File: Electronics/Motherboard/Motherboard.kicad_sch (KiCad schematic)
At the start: 55 parts, among them J1 DX07S024JJ3R1300, J2 Conn_02x10_Odd_Even, M1 AO3400A, M2 AO3400A, M3 AO3400A, U1 AMS1117-3.3, U2 TMC2209_SILENTSTEPSTICK, U3 TMC2209_SILENTSTEPSTICK, U4 TMC2209_SILENTSTEPSTICK, U5 TMC2209_SILENTSTEPSTICK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

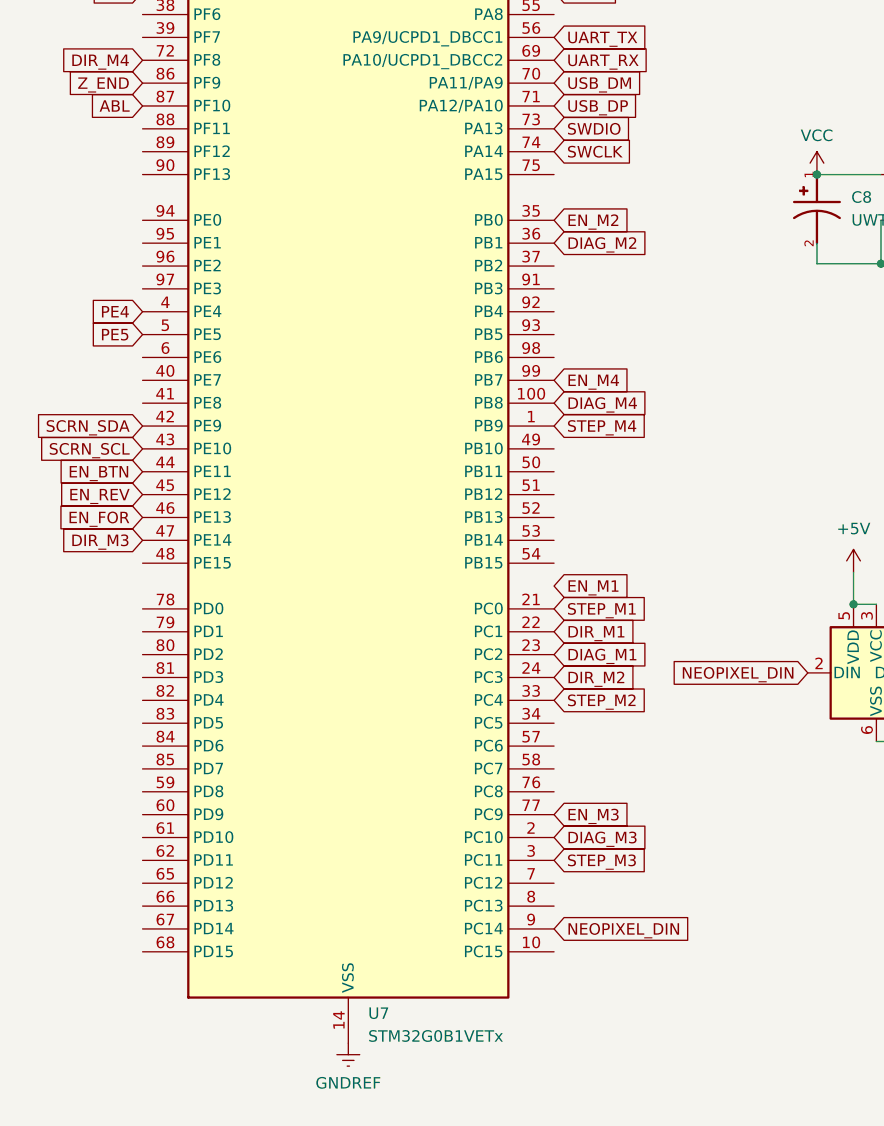
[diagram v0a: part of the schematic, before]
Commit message: tryna make a 2layer versin of this so itd be cheaper, wish me luck lol
uart and driver wirint done
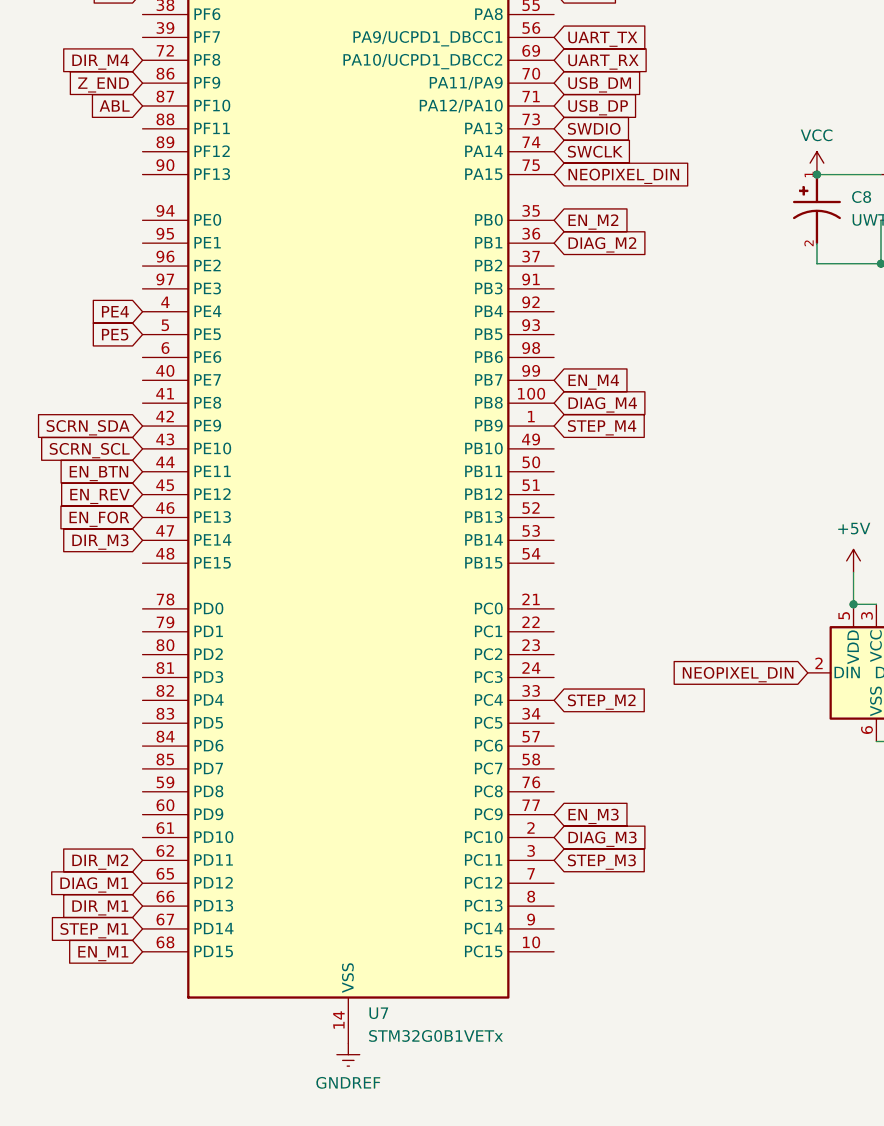
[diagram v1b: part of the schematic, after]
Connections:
- net DIAG_M1: now also U7.65 (PD12); no longer U7.23 (PC2)
- net DIR_M1: now also U7.66 (PD13); no longer U7.22 (PC1)
- net DIR_M2: now also U7.62 (PD11); no longer U7.24 (PC3)
- net EN_M1: now also U7.68 (PD15)
- net NEOPIXEL_DIN: now also U7.75 (PA15); no longer U7.9 (PC14)
- net STEP_M1: now also U7.67 (PD14); no longer U7.21 (PC0)

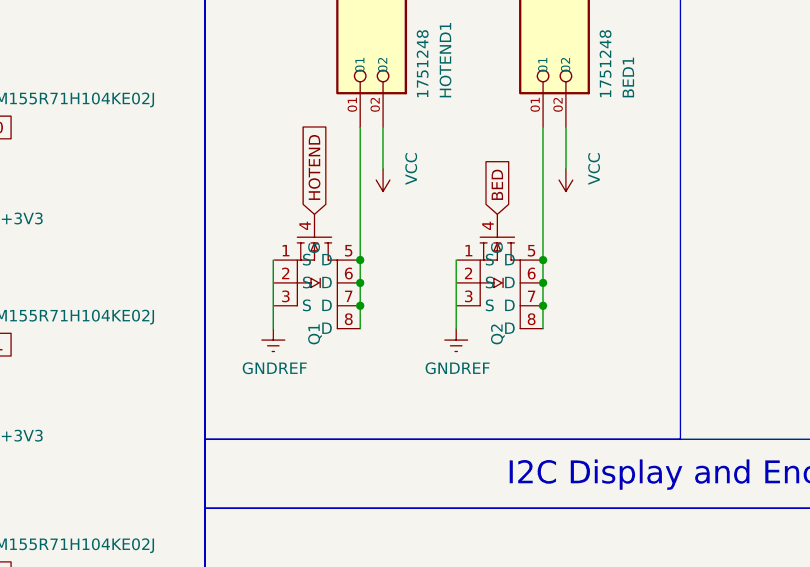
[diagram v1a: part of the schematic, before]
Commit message: fully finished data, partially finished power
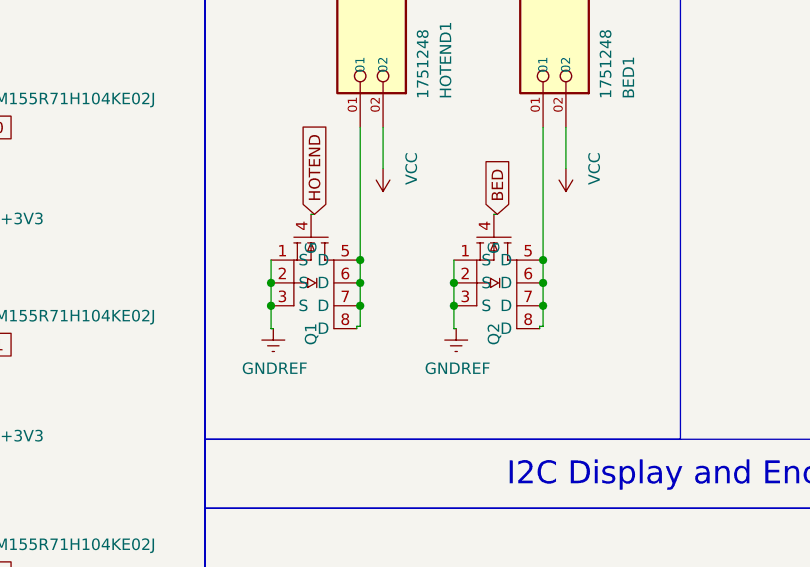
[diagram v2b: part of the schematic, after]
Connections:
- net GNDREF: now also Q1.1 (S), Q1.2 (S), Q1.3 (S), Q2.1 (S), Q2.2 (S), Q2.3 (S)
